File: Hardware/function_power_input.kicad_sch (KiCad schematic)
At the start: 25 parts, among them J2 USB_C_Receptacle_USB2.0_14P, Q1 NMOS, U2 AZ1117-3.3, U3 IP2721

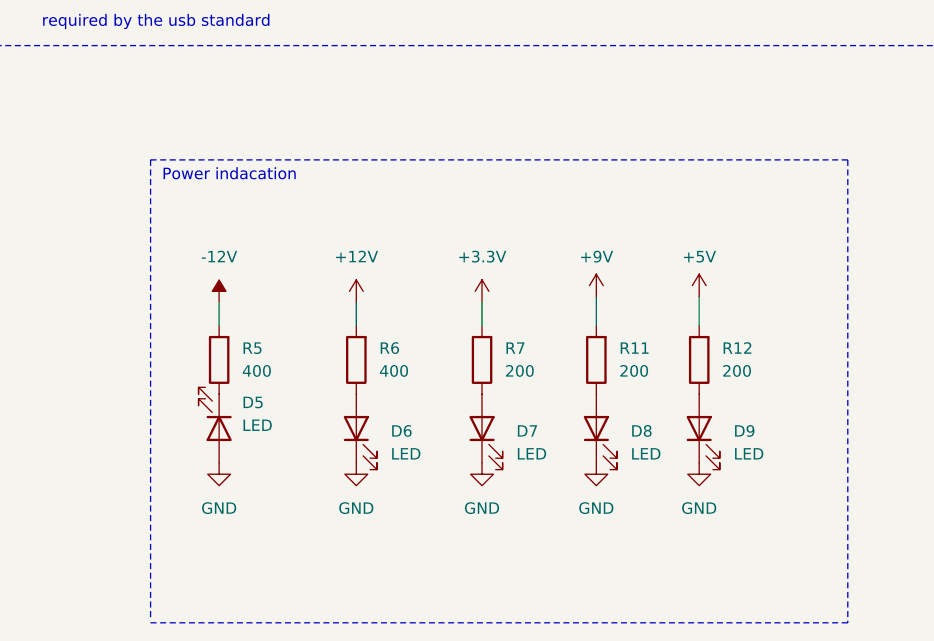
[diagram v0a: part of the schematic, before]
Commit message: Added CODEC symbol, started routing
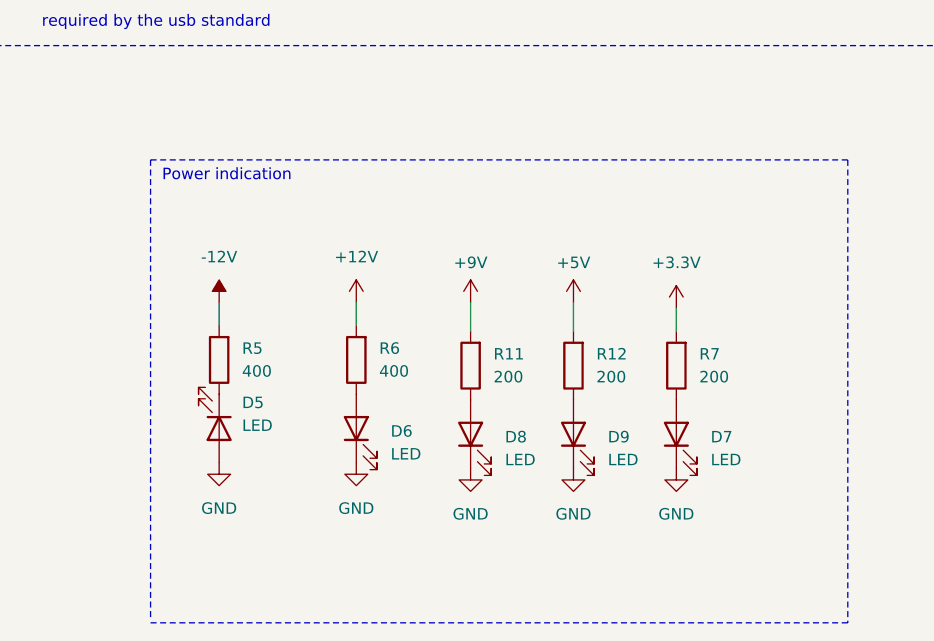
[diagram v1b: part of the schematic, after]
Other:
- note added: "Power indication"
- note removed: "Power indacation"
- moved on the sheet: D7, D8, D9, R11, R12, R7

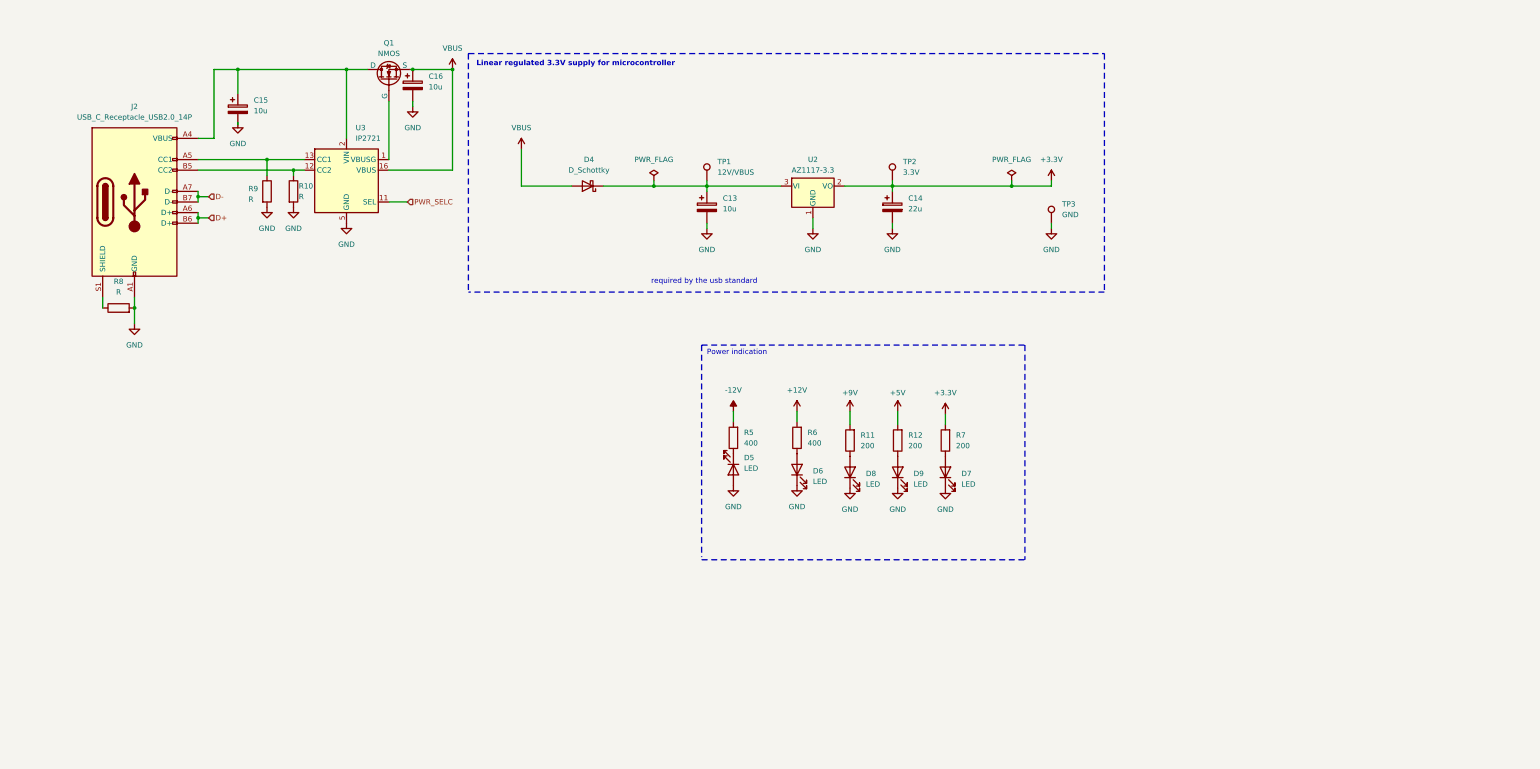
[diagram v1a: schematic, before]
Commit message: added LDO, for 5v, 9, and a dual channel dc/dc converter for dual rail 12v power
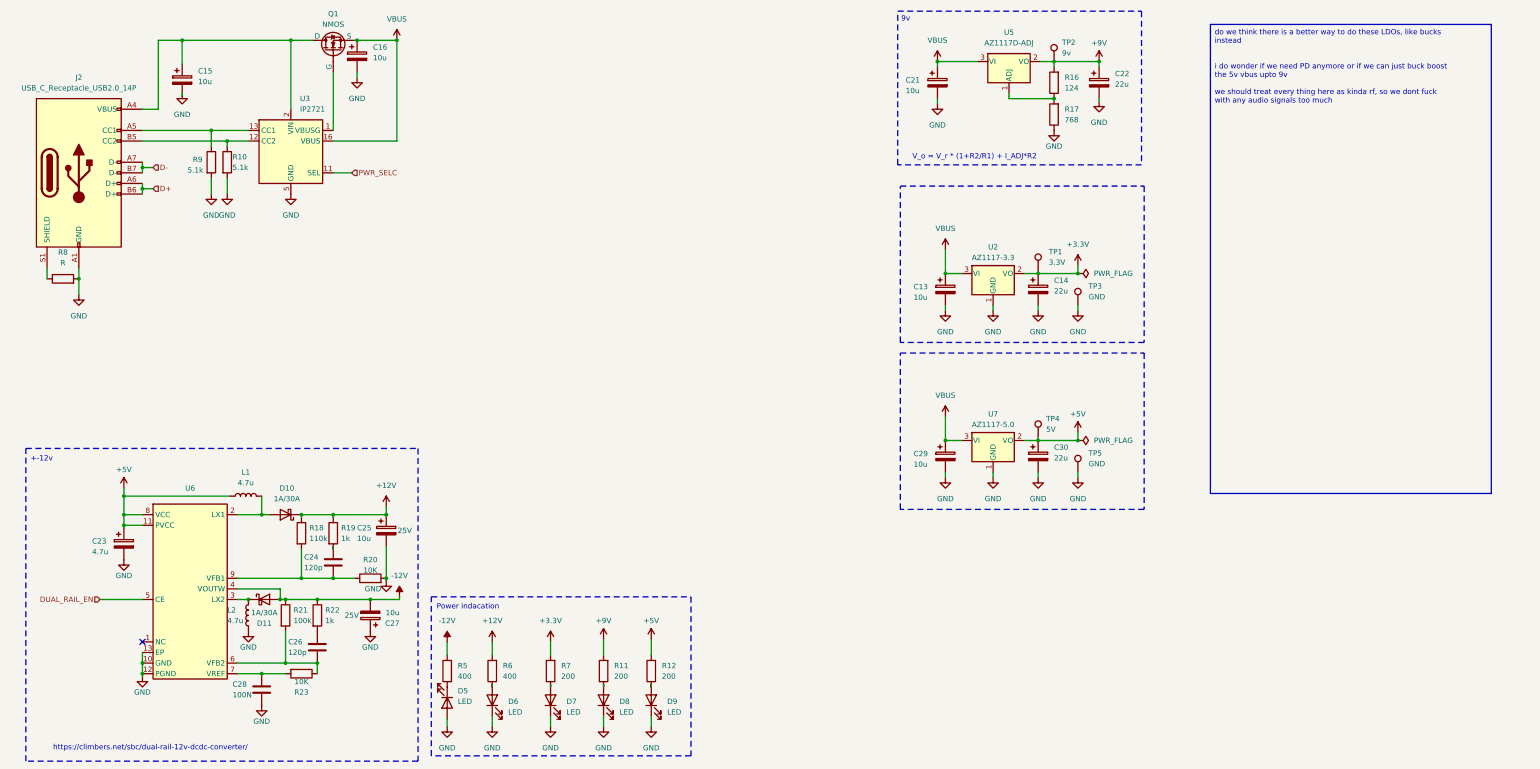
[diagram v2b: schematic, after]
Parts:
- removed D4: D_Schottky, Diode_SMD:D_0805_2012Metric, symbol Device:D_Schottky
- added C21, C25, C27, C29: 10u, Capacitor_SMD:C_0805_2012Metric, symbol Device:C_Polarized
- added C22, C30: 22u, Capacitor_SMD:C_0805_2012Metric, symbol Device:C_Polarized
- added C23: 4.7u, Capacitor_SMD:C_0805_2012Metric, symbol Device:C_Polarized
- added C24, C26: 120p, symbol Device:C
- added C28: 100N, symbol Device:C
- added D10, D11: 1A/30A, symbol Device:D_Schottky
- added L1, L2: 4.7u, symbol Device:L
- added R16: 124, Resistor_SMD:R_0805_2012Metric, symbol Device:R
- added R17: 768, Resistor_SMD:R_0805_2012Metric, symbol Device:R
- added R18: 110k, symbol Device:R
- added R19, R22: 1k, symbol Device:R
- added R20, R23: 10K, symbol Device:R
- added R21: 100k, symbol Device:R
- added TP4: 5V, TestPoint:TestPoint_Pad_D1.5mm, symbol Connector:TestPoint
- added TP5: GND, TestPoint:TestPoint_Pad_D1.5mm, symbol Connector:TestPoint
- added U5: AZ1117D-ADJ, Package_TO_SOT_SMD:TO-252-2, symbol Regulator_Linear:AZ1117D-ADJ
- added U6: ~, DualStepupDC:DFN-12-1EP_2.7x3mm_P0.5mm_EP1.7x2.7mm_HandSolder, symbol CODEC:R1283K0D1
- added U7: AZ1117-5.0, symbol Regulator_Linear:AZ1117-5.0
- R10, R9: value R -> 5.1k
- TP1: value 12V/VBUS -> 3.3V
- TP2: value 3.3V -> 9v
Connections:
- net +12V: now also C25.1, D10.1 (K), R18.1, R19.1
- net +3.3V: now also TP1.1; no longer TP2.1
- net +5V: now also C23.1, C30.1, L1.1, TP4.1, U6.11 (PVCC), U6.8 (VCC), U7.2 (VO)
- net +9V: now also TP2.1, C22.1, R16.2, U5.2 (VO)
- net -12V: now also C27.2, D11.2 (A), R21.1, R22.1, U6.4 (VOUTW)
- net GND: now also C21.2, C22.2, C23.2, C25.2, C27.1, C28.2, C29.2, C30.2, L2.1, R17.1, R20.2, TP5.1, U6.10 (GND), U6.12 (PGND), U6.13 (EP), U7.1 (GND)
- net VBUS: now also C13.1, U2.3 (VI), C21.1, C29.1, U5.3 (VI), U7.3 (VI)
- new net: D11.1 (K), L2.2, U6.3 (LX2)
- new net: C24.2, R18.2, R20.1, U6.9 (VFB1)
- new net: R16.1, R17.2, U5.1 (ADJ)
- new net: D10.2 (A), L1.2, U6.2 (LX1)
- new net: C26.2, R21.2, R23.1, U6.6 (VFB2)
- new net: C26.1, R22.2
- new net: C28.1, R23.2, U6.7 (VREF)
- new net: C24.1, R19.2
- new net DUAL_RAIL_EN: U6.5 (CE)
- no-connect marks 0 -> 1
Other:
- note added: "+-12v"
- note added: "9v"
- note added: "Power indacation"
- note added: "V_o = V_r * (1+R2/R1) + I_ADJ*R2"
- note added: "https://climbers.net/sbc/dual-rail-12v-dcdc-converter/"
- note removed: "Linear regulated 3.3V supply for microcontroller"
- note removed: "Power indication"
- note removed: "required by the usb standard"
- moved on the sheet: C13, C14, C15, C16, D5, D6, D7, D8, D9, J2, Q1, R10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

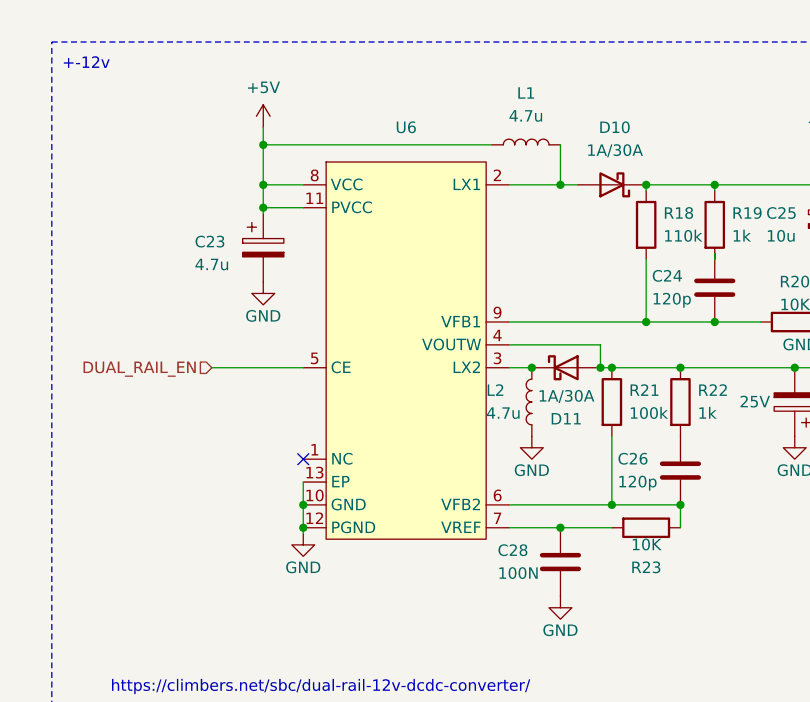
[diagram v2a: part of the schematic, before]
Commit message: CODEC schematics
Missing mic ins and all audio outputs.
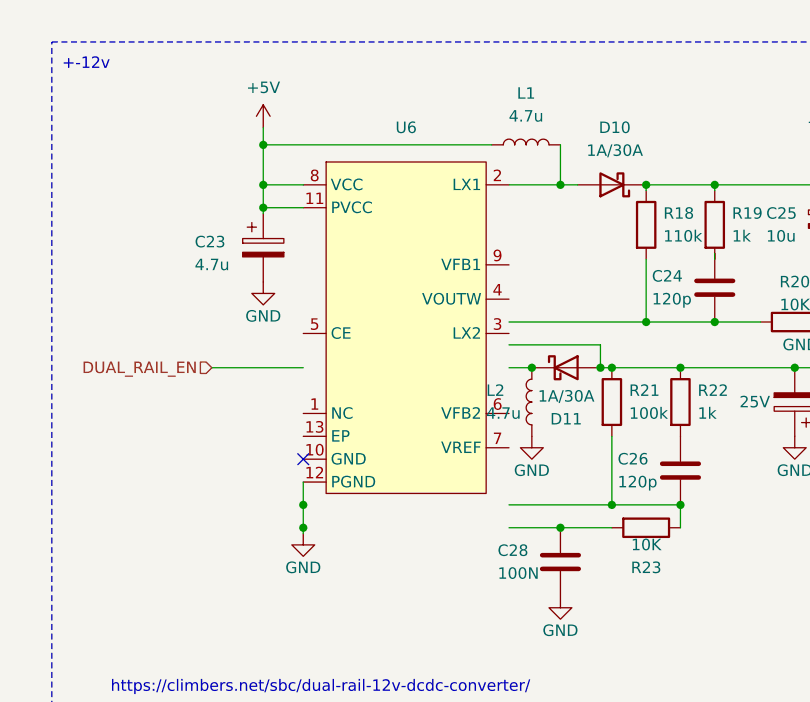
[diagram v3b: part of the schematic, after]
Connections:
- net -12V: no longer U6.4 (VOUTW)
- net DUAL_RAIL_EN: no longer U6.5 (CE)
- net GND: no longer U6.10 (GND), U6.13 (EP)
- net at D11.1 (K), L2.2: no longer U6.3 (LX2)
- net at C24.2, R18.2, R20.1: no longer U6.9 (VFB1)
- net at C26.2, R21.2, R23.1: no longer U6.6 (VFB2)
- net at C28.1, R23.2: no longer U6.7 (VREF)
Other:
- moved on the sheet: U6
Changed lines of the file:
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@@
 			)
 		)
-		(property "Description" ""
+		(property "Description" "Power symbol creates a global label with name \"GND\" , ground"
 			(at 271.78 38.1 0)
 			(effects
@@
 			)
 		)
-		(property "Description" ""
+		(property "Description" "Polarized capacitor"
 			(at 234.95 123.19 0)
 			(effects
@@
 			)
 		)
-		(property "Description" ""
+		(property "Description" "Power symbol creates a global label with name \"GND\" , ground"
 			(at 234.95 128.27 0)
 			(effects
@@
 			)
 		)
-		(property "Description" ""
+		(property "Description" "test point"
 			(at 266.7 127 0)
 			(effects
@@
 			)
 		)
-		(property "Description" ""
+		(property "Description" "Power symbol creates a global label with name \"+12V\""
 			(at 126.365 167.64 0)
 			(effects
@@
 			)
 		)
-		(property "Description" ""
+		(property "Description" "Light emitting diode"
 			(at 153.035 181.61 0)
 			(effects
@@
 			)
 		)
-		(property "Description" ""
+		(property "Description" "Power symbol creates a global label with name \"-12V\""
 			(at 104.14 156.845 0)
 			(effects
@@
 	)
 	(symbol
-		(lib_name "GND_1")
 		(lib_id "power:GND")
 		(at 62.865 60.325 0)
@@
 			)
 		)
-		(property "Description" ""
+		(property "Description" "Power symbol creates a global label with name \"GND\" , ground"
 			(at 257.175 88.265 0)
 			(effects
@@
 			)
 		)
-		(property "Description" ""
+		(property "Description" "Resistor"
 			(at 115.57 174.625 0)
 			(effects
@@
 	)
 	(symbol
-		(lib_name "GND_2")
 		(lib_id "power:GND")
 		(at 71.12 182.88 0)
@@
 			)
 		)
-		(property "Description" ""
+		(property "Description" "Power symbol creates a global label with name \"GND\" , ground"
 			(at 153.035 187.96 0)
 			(effects
@@
 			)
 		)
-		(property "Description" ""
+		(property "Description" "Power symbol creates a global label with name \"GND\" , ground"
 			(at 140.335 187.96 0)
 			(effects
@@
 			)
 		)
-		(property "Description" ""
+		(property "Description" "Power symbol creates a global label with name \"GND\" , ground"
 			(at 126.365 187.96 0)
 			(effects
@@
 			)
 		)
-		(property "Description" ""
+		(property "Description" "Resistor"
 			(at 260.985 41.275 0)
 			(effects
@@
 			)
 		)
-		(property "Description" ""
+		(property "Description" "Polarized capacitor"
 			(at 271.78 33.655 0)
 			(effects
@@
 			)
 		)
-		(property "Description" ""
+		(property "Description" "Light emitting diode"
 			(at 140.335 181.61 0)
 			(effects
@@
 			)
 		)
-		(property "Description" ""
+		(property "Description" "Power symbol creates a global label with name \"VBUS\""
 			(at 234.95 73.66 0)
 			(effects
@@
 			)
 		)
-		(property "Description" ""
+		(property "Description" "1A 20V Fixed LDO Linear Regulator, 3.3V, SOT-89/SOT-223/TO-220/TO-252/TO-263"
 			(at 246.38 79.375 0)
 			(effects
@@
 			)
 		)
-		(property "Description" ""
+		(property "Description" "Power symbol creates a global label with name \"-12V\""
 			(at 115.57 167.64 0)
 			(effects
@@
 			)
 		)
-		(property "Description" ""
+		(property "Description" "Resistor"
 			(at 153.035 174.625 0)
 			(effects
@@
 			)
 		)
-		(property "Description" ""
+		(property "Description" "Power symbol creates a global label with name \"VBUS\""
 			(at 103.505 23.495 0)
 			(effects
@@
 			)
 		)
-		(property "Description" ""
+		(property "Description" "test point"
 			(at 257.175 78.74 0)
 			(effects
@@
 			)
 		)
-		(property "Description" ""
+		(property "Description" "Power symbol creates a global label with name \"GND\" , ground"
 			(at 52.07 36.195 0)
 			(effects
@@
 			)
 		)
-		(property "Description" ""
+		(property "Description" "Resistor"
 			(at 126.365 174.625 0)
 			(effects
@@
 	)
 	(symbol
-		(lib_name "GND_2")
 		(lib_id "power:GND")
 		(at 100.965 153.035 0)
@@
 			)
 		)
-		(property "Description" ""
+		(property "Description" "Light emitting diode"
 			(at 126.365 181.61 0)
 			(effects
@@
 			)
 		)
-		(property "Description" ""
+		(property "Description" "Power symbol creates a global label with name \"+12V\""
 			(at 100.965 135.255 0)
 			(effects
@@
 	)
 	(symbol
-		(lib_name "GND_2")
 		(lib_id "power:GND")
 		(at 38.1 147.955 0)
@@
 			)
 		)
-		(property "Description" ""
+		(property "Description" "Power symbol creates a global label with name \"GND\" , ground"
 			(at 266.7 88.265 0)
 			(effects
@@
 			)
 		)
-		(property "Description" ""
+		(property "Description" "Power symbol creates a global label with name \"GND\" , ground"
 			(at 246.38 88.265 0)
 			(effects
@@
 			)
 		)
-		(property "Description" ""
+		(property "Description" "Polarized capacitor"
 			(at 52.07 33.02 0)
 			(effects
@@
 			)
 		)
-		(property "Description" ""
+		(property "Description" "Special symbol for telling ERC where power comes from"
 			(at 266.7 79.375 0)
 			(effects
@@
 	)
 	(symbol
-		(lib_name "GND_2")
 		(lib_id "power:GND")
 		(at 97.155 165.1 0)
@@
 			)
 		)
-		(property "Description" ""
+		(property "Description" "test point"
 			(at 260.985 28.575 0)
 			(effects
@@
 			)
 		)
-		(property "Description" ""
+		(property "Description" "Power symbol creates a global label with name \"GND\" , ground"
 			(at 115.57 187.96 0)
 			(effects
@@
 	)
 	(symbol
-		(lib_name "GND_1")
 		(lib_id "power:GND")
 		(at 59.055 60.325 0)
@@
 			)
 		)
-		(property "Description" ""
+		(property "Description" "Power symbol creates a global label with name \"+3.3V\""
 			(at 266.7 77.47 0)
 			(effects
@@
 			)
 		)
-		(property "Description" ""
+		(property "Description" "Power symbol creates a global label with name \"GND\" , ground"
 			(at 93.98 32.385 0)
 			(effects
@@
 			)
 		)
-		(property "Description" ""
+		(property "Description" "Power symbol creates a global label with name \"VBUS\""
 			(at 234.95 113.665 0)
 			(effects
@@
 			)
 		)
-		(property "Description" ""
+		(property "Description" "Polarized capacitor"
 			(at 97.155 161.29 0)
 			(effects
@@
 			)
 		)
-		(property "Description" ""
+		(property "Description" "Power symbol creates a global label with name \"GND\" , ground"
 			(at 257.175 128.27 0)
 			(effects
@@
 			)
 		)
-		(property "Description" ""
+		(property "Description" "Polarized capacitor"
 			(at 93.98 27.305 0)
 			(effects
@@
 			)
 		)
-		(property "Description" ""
+		(property "Description" "Polarized capacitor"
 			(at 234.95 83.185 0)
 			(effects
@@
 	)
 	(symbol
-		(lib_name "GND_2")
 		(lib_id "power:GND")
 		(at 67.945 165.1 0)
@@
 			)
 		)
-		(property "Description" ""
+		(property "Description" "Polarized capacitor"
 			(at 233.045 33.655 0)
 			(effects
@@
 			)
 		)
-		(property "Description" ""
+		(property "Description" "Polarized capacitor"
 			(at 38.1 144.145 0)
 			(effects
@@
 	)
 	(symbol
-		(lib_name "GND_2")
 		(lib_id "power:GND")
 		(at 42.545 175.895 0)
@@
 			)
 		)
-		(property "Description" ""
+		(property "Description" "Power symbol creates a global label with name \"GND\" , ground"
 			(at 260.985 45.085 0)
 			(effects
@@
 	)
 	(symbol
-		(lib_name "GND_1")
 		(lib_id "power:GND")
 		(at 27.305 84.455 0)
@@
 			)
 		)
-		(property "Description" ""
+		(property "Description" "Light emitting diode"
 			(at 164.465 181.61 0)
 			(effects
@@
 	)
 	(symbol
-		(lib_name "GND_1")
 		(lib_id "power:GND")
 		(at 78.105 60.325 0)
@@
 			)
 		)
-		(property "Description" ""
+		(property "Description" "Resistor"
 			(at 140.335 174.625 0)
 			(effects
@@
 			)
 		)
-		(property "Description" ""
+		(property "Description" "Polarized capacitor"
 			(at 100.965 140.97 0)
 			(effects
@@
 			)
 		)
-		(property "Description" ""
+		(property "Description" "Resistor"
 			(at 260.985 33.655 0)
 			(effects
@@
 			)
 		)
-		(property "Description" ""
+		(property "Description" "test point"
 			(at 257.175 118.745 0)
 			(effects
@@
 			)
 		)
-		(property "Description" ""
+		(property "Description" "Power symbol creates a global label with name \"+3.3V\""
 			(at 140.335 167.64 0)
 			(effects
@@
 			)
 		)
-		(property "Description" ""
+		(property "Description" "Power symbol creates a global label with name \"GND\" , ground"
 			(at 246.38 128.27 0)
 			(effects
@@
 			)
 		)
-		(property "Description" ""
+		(property "Description" "Special symbol for telling ERC where power comes from"
 			(at 266.7 119.38 0)
 			(effects
@@
 			)
 		)
-		(property "Description" ""
+		(property "Description" "Polarized capacitor"
 			(at 257.175 83.185 0)
 			(effects
@@
 			)
 		)
-		(property "Description" ""
+		(property "Description" "Resistor"
 			(at 164.465 174.625 0)
 			(effects
@@
 			)
 		)
-		(property "Description" ""
+		(property "Description" "Power symbol creates a global label with name \"GND\" , ground"
 			(at 233.045 38.735 0)
 			(effects
@@
 			)
 		)
-		(property "Description" ""
+		(property "Description" "Power symbol creates a global label with name \"VBUS\""
 			(at 233.045 28.575 0)
 			(effects
@@
 			)
 		)
-		(property "Description" ""
+		(property "Description" "Polarized capacitor"
 			(at 257.175 123.19 0)
 			(effects
@@
 			)
 		)
-		(property "Description" ""
+		(property "Description" "Power symbol creates a global label with name \"GND\" , ground"
 			(at 164.465 187.96 0)
 			(effects
@@
 			)
 		)
-		(property "Description" ""
+		(property "Description" "test point"
 			(at 266.7 86.995 0)
 			(effects
@@
 			)
 		)
-		(property "Description" ""
+		(property "Description" "Power symbol creates a global label with name \"GND\" , ground"
 			(at 234.95 88.265 0)
 			(effects
@@
 			)
 		)
-		(property "Description" ""
+		(property "Description" "Power symbol creates a global label with name \"GND\" , ground"
 			(at 266.7 128.27 0)
 			(effects
@@
 			)
 		)
-		(property "Description" ""
+		(property "Description" "Light emitting diode"
 			(at 115.57 182.245 0)
 			(effects
